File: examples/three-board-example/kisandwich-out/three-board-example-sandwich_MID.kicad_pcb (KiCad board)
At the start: 6 copper layers, 55 x 55.8 mm, 1 part

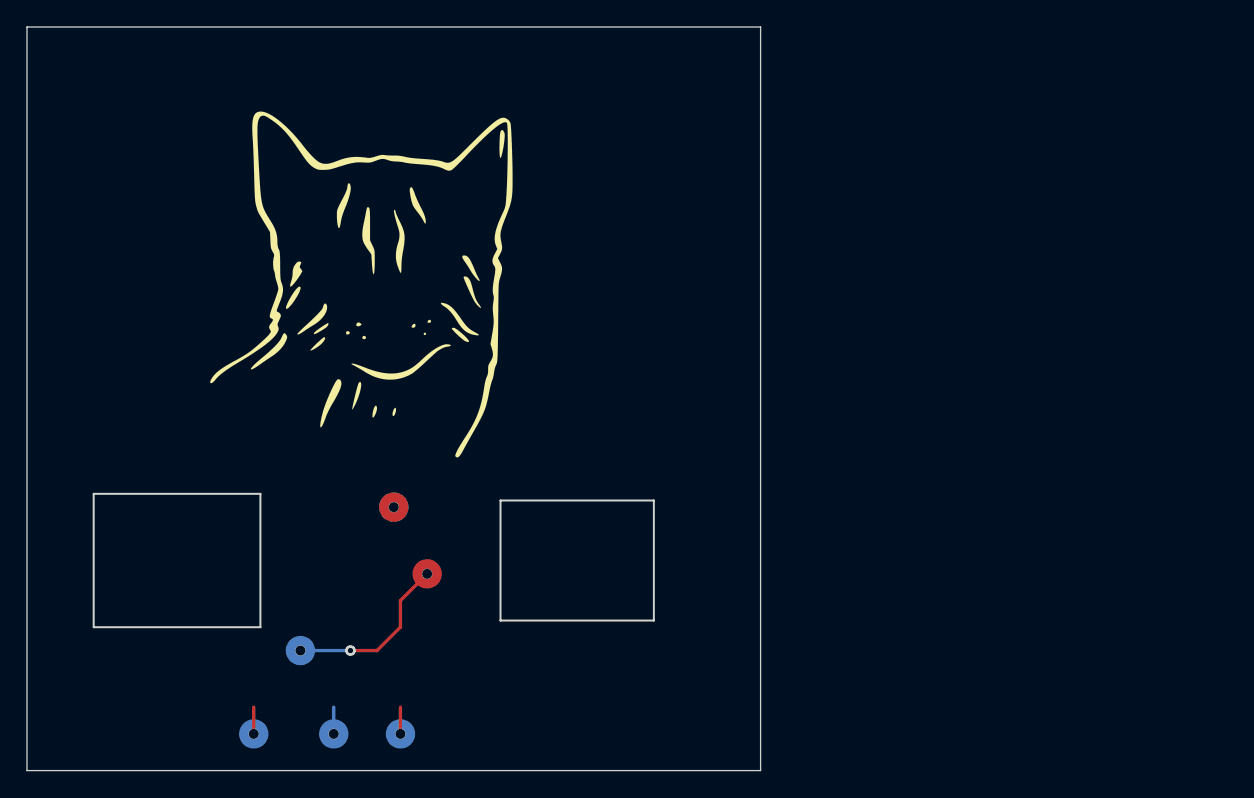
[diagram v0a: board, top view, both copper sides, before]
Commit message: Made 3D representations. Changed speaker to being placed on midboard. Checked heights
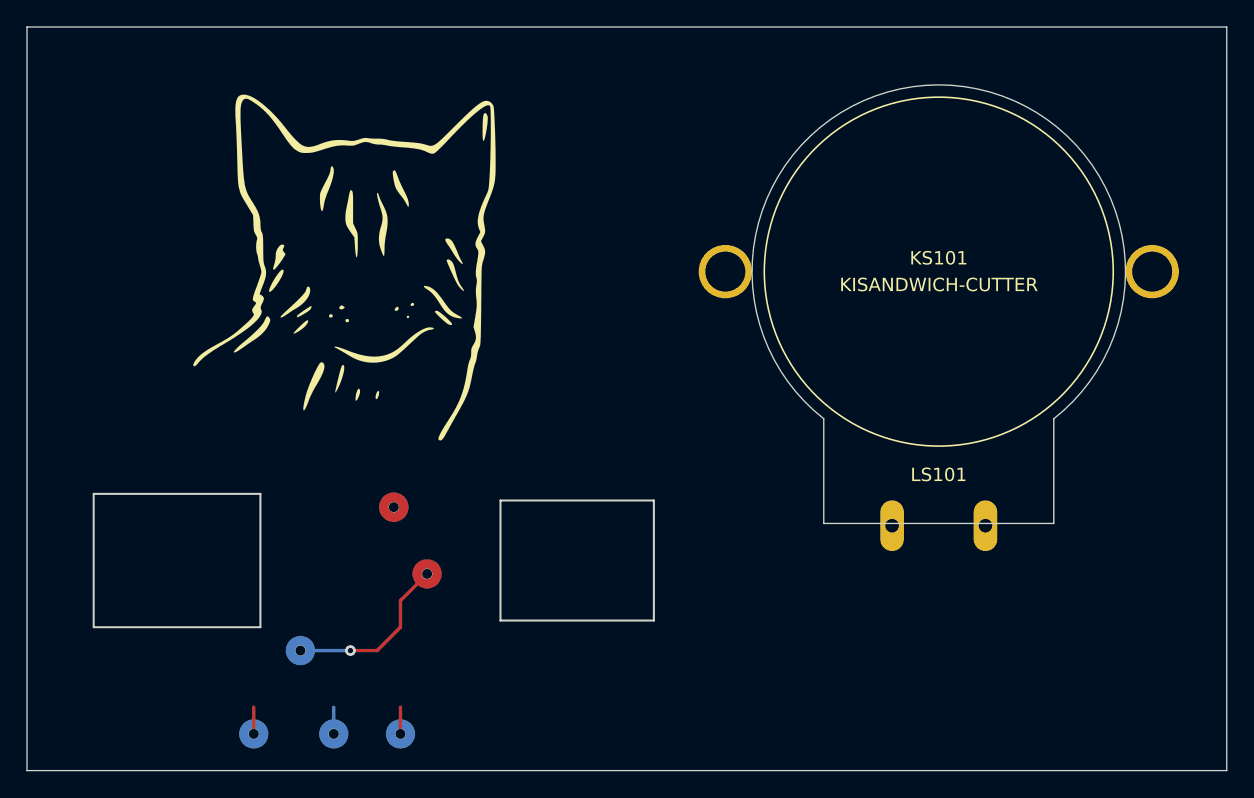
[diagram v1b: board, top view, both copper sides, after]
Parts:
- added KS101: KISANDWICH-CUTTER, Alex_Connectors:CUI-speaker-3layer-tight, F.Cu at (213.4, 53.3)
- added LS101: KISANDWICH-MIDBOARD, Alex_Connectors:Speaker_CUI_CLS0281MAE_embedded, F.Cu at (213.4, 53.3)
- moved G1 1.80 mm to (168.7, 53.0)
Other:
- board size 55 x 55.8 mm -> 89.9 x 55.8 mm
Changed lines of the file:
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@@
     (tracks 15)
     (zones 0)
-    (modules 1)
-    (nets 4)
+    (modules 3)
+    (nets 6)
   )
   (page A4)
@@
   (net 2 "Net-(U1-Pad2)")
   (net 3 "Net-(U1-Pad1)")
+  (net 4 "Net-(LS101-Pad1)")
+  (net 5 "Net-(LS101-Pad2)")
   (net_class Default "This is the default net class."
     (clearance 0.2)
@@
     (uvia_dia 0.3)
     (uvia_drill 0.1)
+    (add_net "Net-(LS101-Pad1)")
+    (add_net "Net-(LS101-Pad2)")
     (add_net "Net-(U1-Pad1)")
     (add_net "Net-(U1-Pad2)")
     (add_net "Net-(U1-Pad3)")
   )
+  (module Alex_Connectors:CUI-speaker-3layer-tight (layer F.Cu)
+    (at 213.36 53.34 180)
+    (descr "STD_v2_allSketches StepUp generated footprint")
+    (attr smd)
+    (fp_text reference KS101 (at 0 1) (layer F.SilkS)
+      (effects (font (size 1 1) (thickness 0.15)))
+    )
+    (fp_text value KISANDWICH-CUTTER (at 0 -1) (layer F.SilkS)
+      (effects (font (size 1 1) (thickness 0.15)))
+    )
+    (fp_line (start -8.624 -18.88) (end 8.624 -18.88) (layer Edge.Cuts) (width 0.1))
+    (fp_line (start 8.624 -18.88) (end 8.624 -11.029) (layer Edge.Cuts) (width 0.1))
+    (fp_line (start -8.624 -18.88) (end -8.624 -11.029) (layer Edge.Cuts) (width 0.1))
+    (fp_text user %R (at 0 1) (layer F.Fab)
+      (effects (font (size 1 1) (thickness 0.15)))
+    )
+    (fp_text user "EDIT PAD NUMBERS" (at 0 -2) (layer Cmts.User)
+      (effects (font (size 1 1) (thickness 0.2) italic))
+    )
+    (fp_arc (start 0 0) (end -8.624 -11.029) (angle -283.955) (layer Edge.Cuts) (width 0.1))
+  )
+  (module Alex_Connectors:Speaker_CUI_CLS0281MAE_embedded (layer F.Cu)
+    (at 213.36 53.34 180)
+    (fp_text reference LS101 (at 0 -15.24) (layer F.SilkS)
+      (effects (font (size 1 1) (thickness 0.15)))
+    )
+    (fp_text value KISANDWICH-MIDBOARD (at 0 15.24) (layer F.Fab)
+      (effects (font (size 1 1) (thickness 0.15)))
+    )
+    (fp_circle (center 0 0) (end 14.00048 0) (layer B.CrtYd) (width 0.12))
+    (fp_circle (center 0 0) (end 12.954 0) (layer Dwgs.User) (width 0.12))
+    (fp_line (start -18.415 -1.3335) (end -9.3345 -10.4775) (layer B.CrtYd) (width 0.12))
+    (fp_line (start -18.383618 1.365618) (end -9.271 10.541) (layer B.CrtYd) (width 0.12))
+    (fp_line (start 18.383618 -1.365618) (end 9.271 -10.541) (layer B.CrtYd) (width 0.12))
+    (fp_line (start 18.415 1.3335) (end 9.3345 10.4775) (layer B.CrtYd) (width 0.12))
+    (fp_circle (center 0 0) (end 13.081 0) (layer F.SilkS) (width 0.12))
+    (fp_line (start 18.383618 -1.365618) (end 9.271 -10.541) (layer B.SilkS) (width 0.12))
+    (fp_circle (center 0 0) (end 14.00048 0) (layer B.SilkS) (width 0.12))
+    (fp_line (start -18.383618 1.365618) (end -9.271 10.541) (layer B.SilkS) (width 0.12))
+    (fp_line (start 18.415 1.3335) (end 9.3345 10.4775) (layer B.SilkS) (width 0.12))
+    (fp_line (start -18.415 -1.3335) (end -9.3345 -10.4775) (layer B.SilkS) (width 0.12))
+    (fp_circle (center 0 0) (end 13.97 0) (layer F.CrtYd) (width 0.12))
+    (fp_arc (start -17.018 0) (end -18.414999 -1.333499) (angle -88.7) (layer B.SilkS) (width 0.12))
+    (fp_arc (start 17.018 0) (end 18.414999 1.333499) (angle -88.7) (layer B.SilkS) (width 0.12))
+    (fp_arc (start 17.018 0) (end 18.414999 1.333499) (angle -88.66778015) (layer B.CrtYd) (width 0.12))
+    (fp_arc (start -17.018 0) (end -18.414999 -1.333499) (angle -88.66778015) (layer B.CrtYd) (width 0.12))
+    (pad 1 thru_hole oval (at -3.50012 -19.05 270) (size 3.81 1.778) (drill 1.016) (layers *.Cu *.Mask)
+      (net 4 "Net-(LS101-Pad1)"))
+    (pad 2 thru_hole oval (at 3.50012 -19.05 270) (size 3.81 1.778) (drill 1.016) (layers *.Cu *.Mask)
+      (net 5 "Net-(LS101-Pad2)"))
+    (pad "" thru_hole circle (at 16.002 0 180) (size 4 4) (drill 2.999999) (layers *.Cu *.Mask))
+    (pad "" thru_hole circle (at -16.002 0 180) (size 4 4) (drill 2.999999) (layers *.Cu *.Mask))
+    (model ${ATAIT_3D_DIR}/CUI_DEVICES_CLS0281MAE-L152.step
+      (offset (xyz 0 0 1.3))
+      (scale (xyz 1 1 1))
+      (rotate (xyz 90 0 0))
+    )
+  )
   (module Alex_Graphics:cat_02 (layer F.Cu)
-    (at 170 54.25)
+    (at 168.73 52.98)
     (descr "Imported from cat.svg")
     (tags svg2mod)
@@
   (gr_line (start 150 70) (end 162.5 70) (layer Edge.Cuts) (width 0.15))
   (gr_line (start 145 90.75) (end 145 35) (layer Edge.Cuts) (width 0.05))
-  (gr_line (start 200 90.75) (end 145 90.75) (layer Edge.Cuts) (width 0.05))
-  (gr_line (start 200 35) (end 200 90.75) (layer Edge.Cuts) (width 0.05))
-  (gr_line (start 145 35) (end 200 35) (layer Edge.Cuts) (width 0.05))
+  (gr_line (start 234.95 90.75) (end 145 90.75) (layer Edge.Cuts) (width 0.05))
+  (gr_line (start 234.95 35) (end 234.95 90.75) (layer Edge.Cuts) (width 0.05))
+  (gr_line (start 145 35) (end 234.95 35) (layer Edge.Cuts) (width 0.05))
   (via (at 172.5 71) (size 0.7875) (drill 0.75) (layers F.Cu B.Cu) (net 1))
   (via (at 165.5 81.75) (size 0.7875) (drill 0.75) (layers F.Cu B.Cu) (net 2))

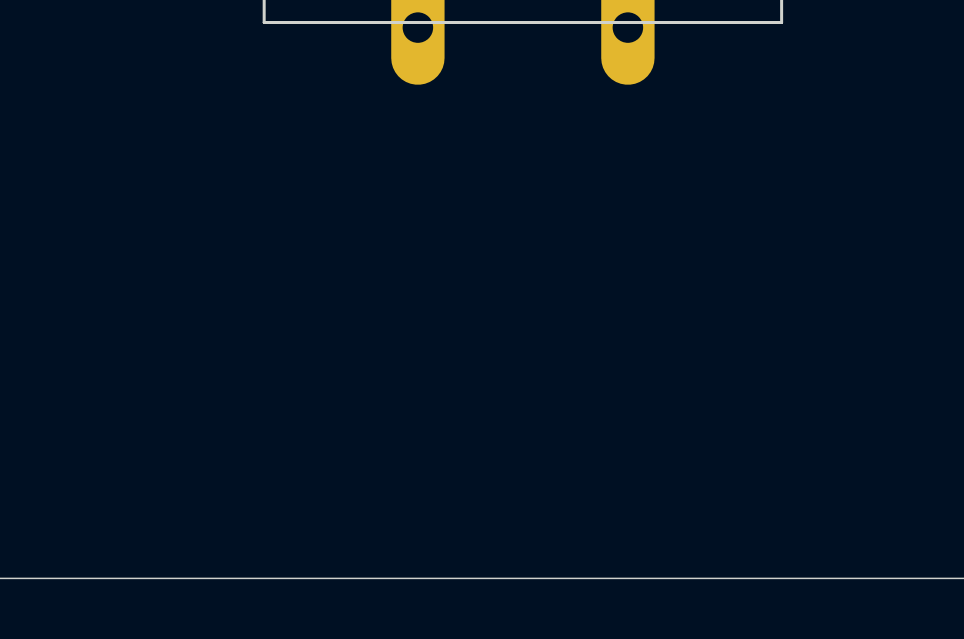
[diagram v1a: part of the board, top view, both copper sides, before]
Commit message: Also processing copper that is in cutter modules
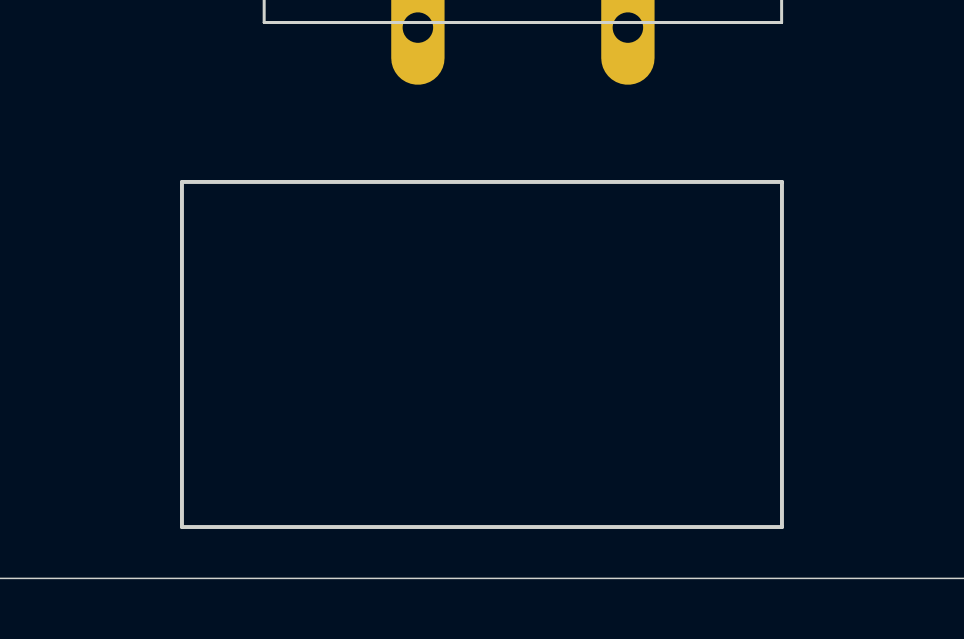
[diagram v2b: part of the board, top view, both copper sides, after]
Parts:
- added svg2mod: KISANDWICH-CUTTER, Alex_Sandwiches:light-hole, F.Cu at (201.9, 77.5)
